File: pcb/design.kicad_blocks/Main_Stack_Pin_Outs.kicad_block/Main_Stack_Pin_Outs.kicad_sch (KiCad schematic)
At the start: 6 parts, among them J10 1528-1112-ND, J5 1528-1112-ND, J6 1528-1112-ND, J7 1528-1112-ND, J8 1528-1112-ND, J9 1528-1112-ND

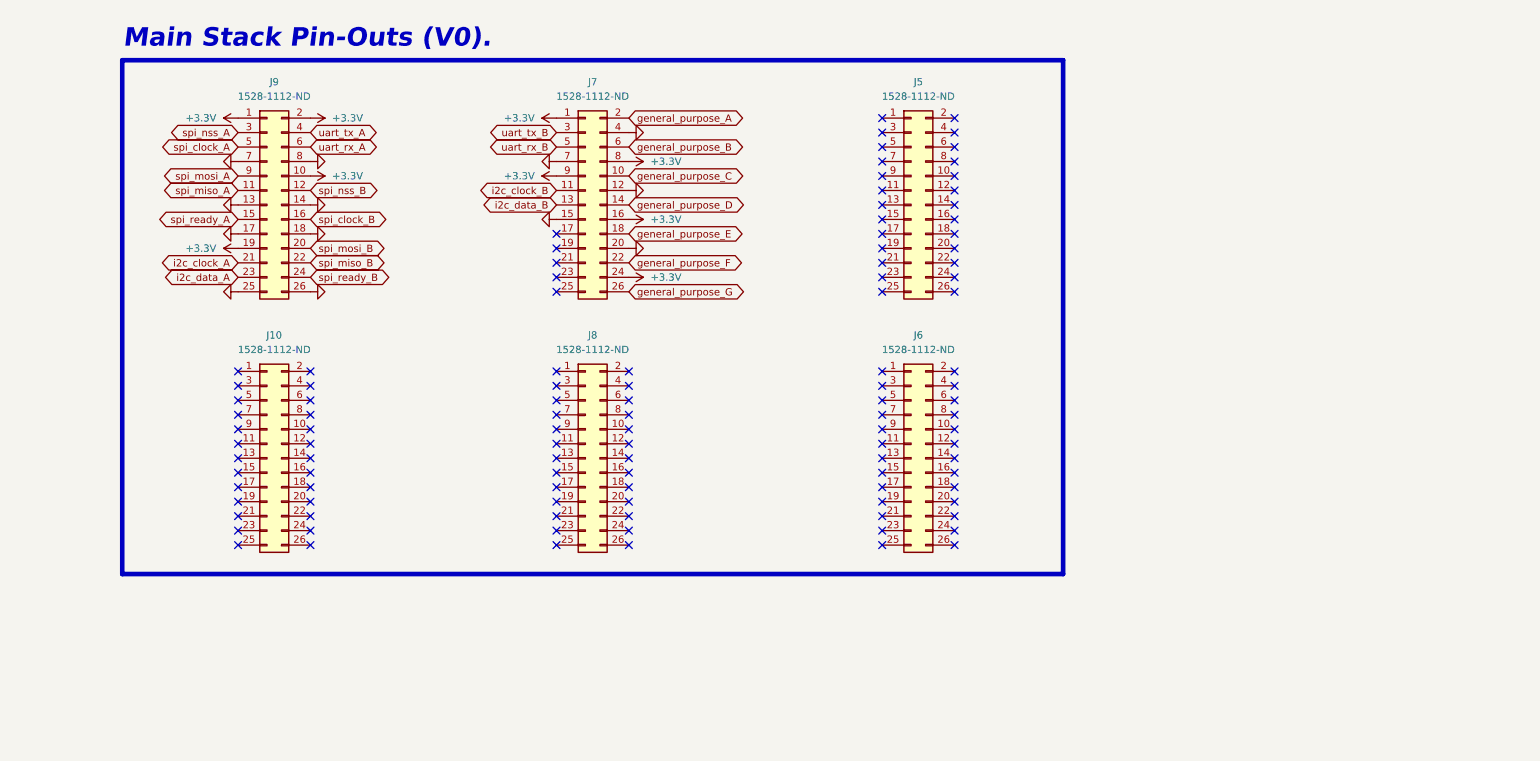
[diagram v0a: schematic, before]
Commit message: Using a different stack-up connector.
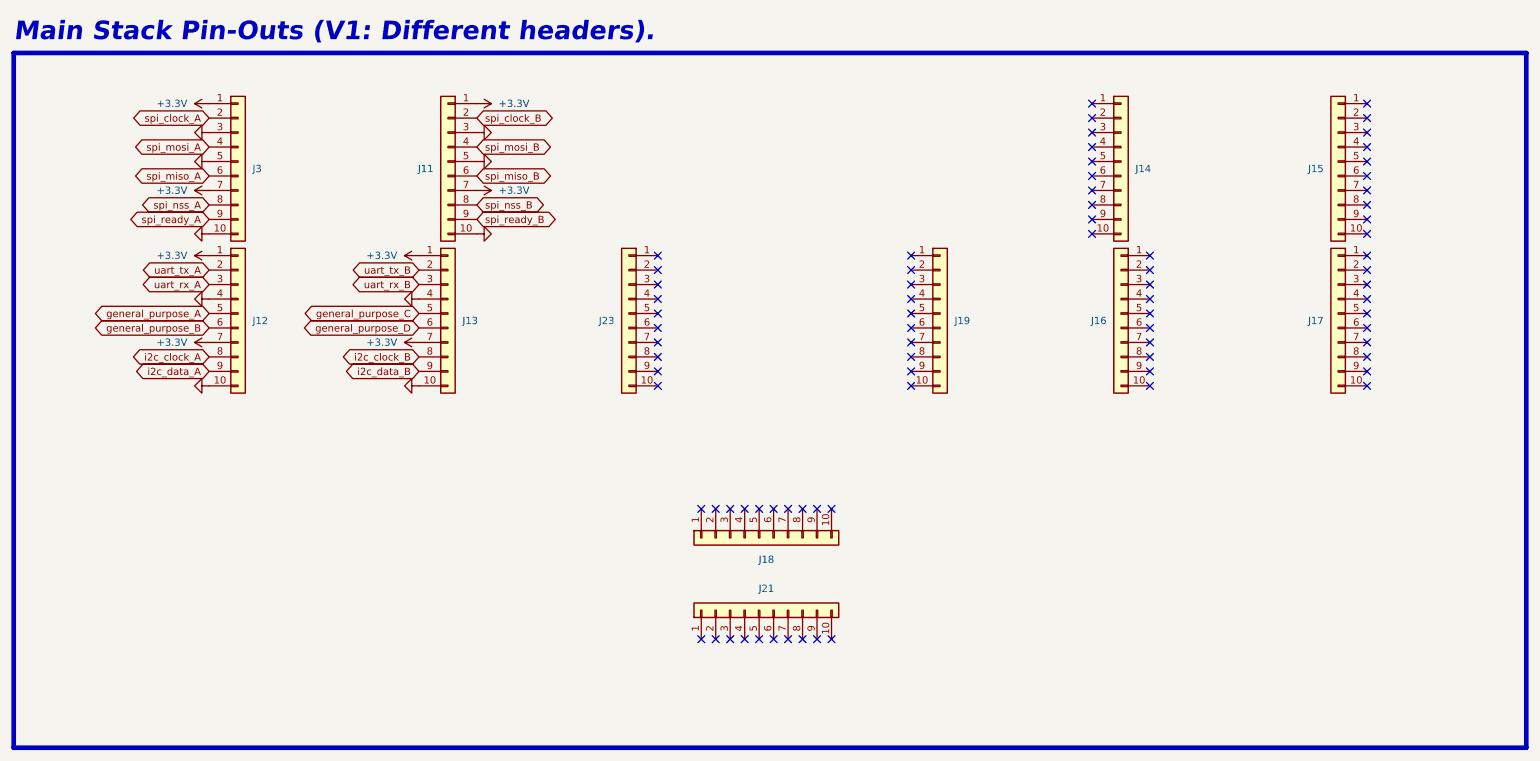
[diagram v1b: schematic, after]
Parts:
- removed J10, J5, J6, J7, J8, J9: 1528-1112-ND, Connector_PinSocket_2.54mm:PinSocket_2x13_P2.54mm_Vertical, symbol Connector_Generic:Conn_02x13_Odd_Even
- added J11, J12, J13, J14, J15, J16, J17, J18, J19, J21, J23, J3: Conn_01x10, pcb:Stack_Connector_1x10, symbol Connector_Generic:Conn_01x10
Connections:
- net +3.3V: now also J11.1 (Pin_1), J11.7 (Pin_7), J12.1 (Pin_1), J12.7 (Pin_7), J13.1 (Pin_1), J13.7 (Pin_7), J3.1 (Pin_1), J3.7 (Pin_7)
- net GND: now also J11.10 (Pin_10), J11.3 (Pin_3), J11.5 (Pin_5), J12.10 (Pin_10), J12.4 (Pin_4), J13.10 (Pin_10), J13.4 (Pin_4), J3.10 (Pin_10), J3.3 (Pin_3), J3.5 (Pin_5)
- net general_purpose_A: now also J12.5 (Pin_5)
- net general_purpose_B: now also J12.6 (Pin_6)
- net general_purpose_C: now also J13.5 (Pin_5)
- net general_purpose_D: now also J13.6 (Pin_6)
- net i2c_clock_A: now also J12.8 (Pin_8)
- net i2c_clock_B: now also J13.8 (Pin_8)
- net i2c_data_A: now also J12.9 (Pin_9)
- net i2c_data_B: now also J13.9 (Pin_9)
- net spi_clock_A: now also J3.2 (Pin_2)
- net spi_clock_B: now also J11.2 (Pin_2)
- net spi_miso_A: now also J3.6 (Pin_6)
- net spi_miso_B: now also J11.6 (Pin_6)
- net spi_mosi_A: now also J3.4 (Pin_4)
- net spi_mosi_B: now also J11.4 (Pin_4)
- net spi_nss_A: now also J3.8 (Pin_8)
- net spi_nss_B: now also J11.8 (Pin_8)
- net spi_ready_A: now also J3.9 (Pin_9)
- net spi_ready_B: now also J11.9 (Pin_9)
- net uart_rx_A: now also J12.3 (Pin_3)
- net uart_rx_B: now also J13.3 (Pin_3)
- net uart_tx_A: now also J12.2 (Pin_2)
- net uart_tx_B: now also J13.2 (Pin_2)
- no-connect marks 109 -> 80
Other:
- note added: "Main Stack Pin-Outs (V1: Different headers)."
- note removed: "Main Stack Pin-Outs (V0)."
